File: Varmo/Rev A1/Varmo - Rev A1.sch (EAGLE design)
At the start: 73 parts, among them U1 ATMEGA328, U2 SN74LVC2G17DBVR, U3 SN74LVC2G17DBVR, U4 90814-0210, U5 90814-0210, U6 IRLML6344TRPBF, X1 NC5MAH, X2 SMKDSP_1,5/3, X3 SMKDSP_1,5/2, X4 SMKDSP_1,5/2, Y1 8MHz

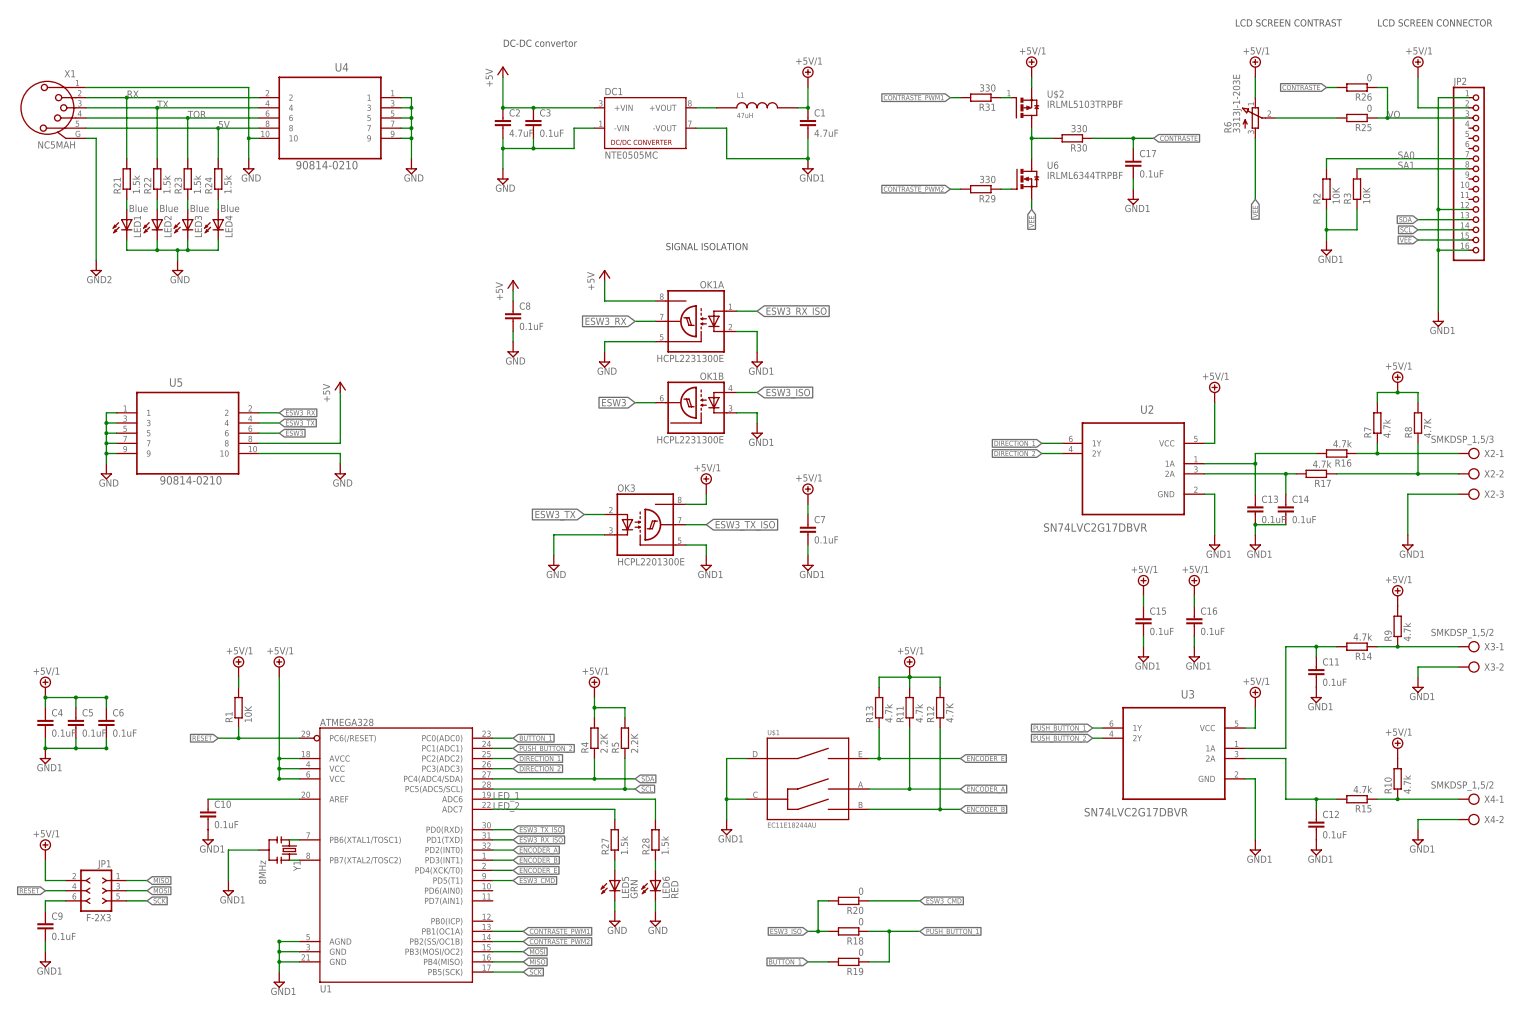
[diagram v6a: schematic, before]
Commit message: Update board of Varmo Rev 1, Update dc-dc-converter library
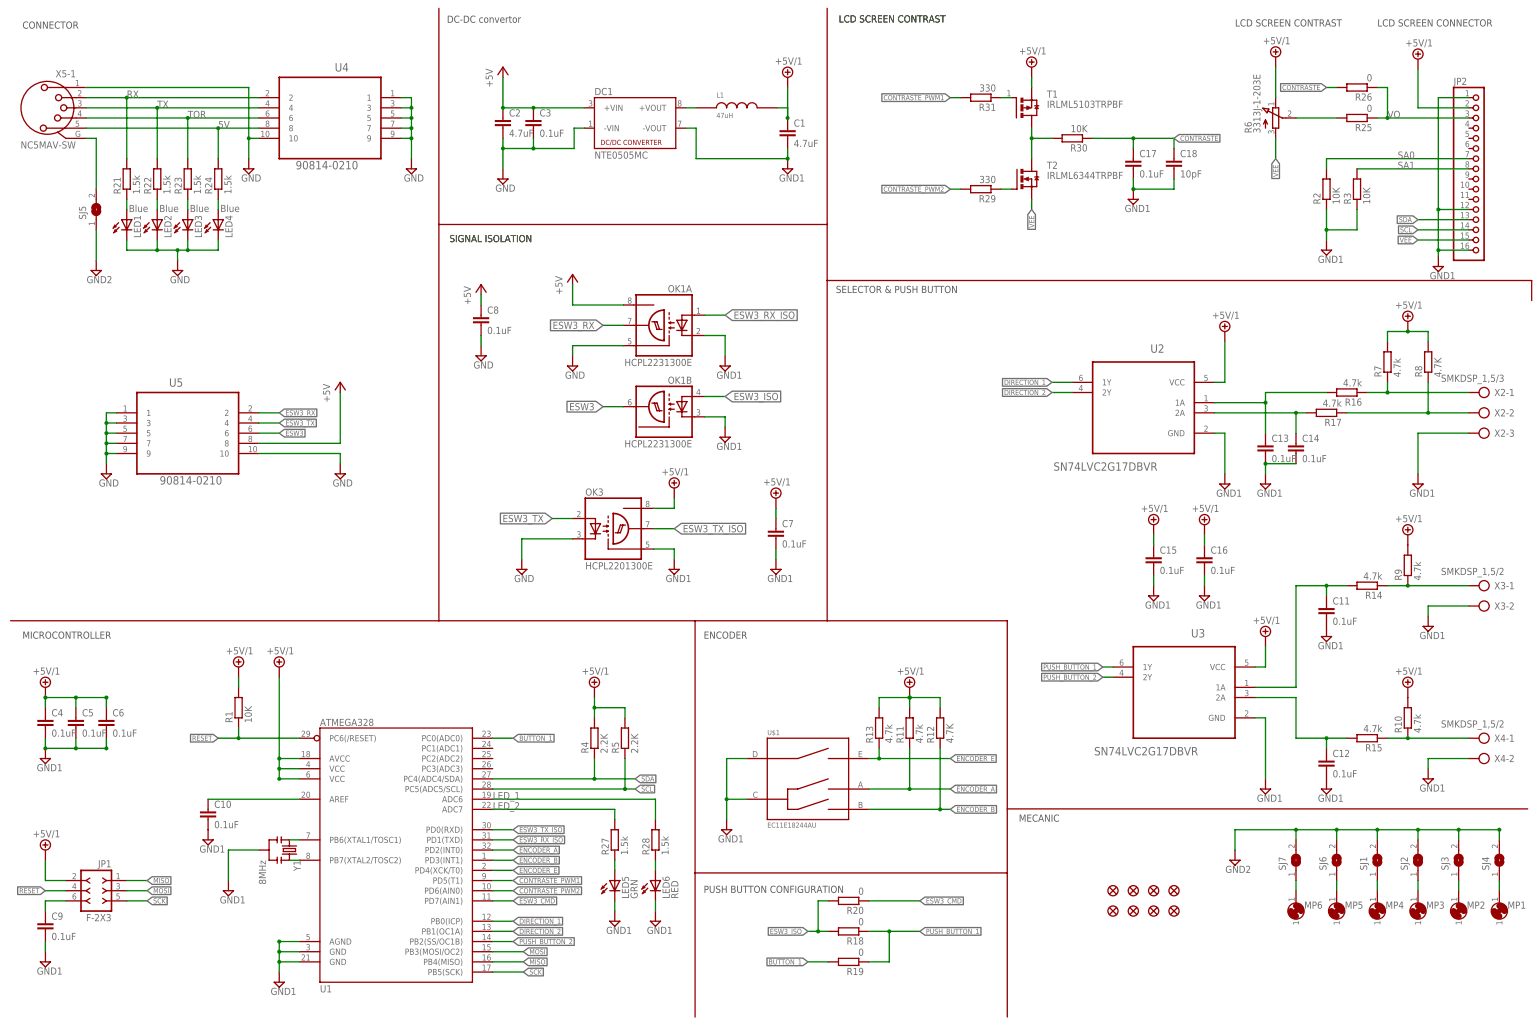
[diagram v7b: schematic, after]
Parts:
- removed X1: NC5MAH, con-neutrik_ag:NC5MAH
- added C18: 10pF, rcl:C-EUC0603
- added JP10, JP3, JP4, JP5, JP6, JP7, JP8, JP9: FIDUCIAL1X2, SparkFun:FIDUCIAL1X2
- added MP1, MP2, MP3, MP4, MP5, MP6: MOUNT-PAD3,0, holes:MOUNT-PAD3,0
- added SJ1, SJ2, SJ3, SJ4, SJ5, SJ6, SJ7: (no value), jumper:SJ
- added X5: NC5MAV-SW, con-neutrik_ag:NC5MAV-SW
- R30: value 330 -> 10K
- renumbered U$2 to T1, U6 to T2
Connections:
- new net 1: MP1.1, MP2.1, MP3.1, MP4.1, MP5.1, MP6.1, SJ1.1, SJ2.1, SJ3.1, SJ4.1, SJ6.1, SJ7.1
- new net N$23: SJ5.2, X5-1.G
- net 5V: now also X5-1.5; no longer X1.5
- net CONTRASTE: now also C18.1
- net CONTRASTE_PWM1: now also U1.PD5(T1); no longer U1.PB1(OC1A)
- net CONTRASTE_PWM2: now also U1.PD6(AIN0); no longer U1.PB2(SS/OC1B)
- net DIRECTION_1: now also U1.PB0(ICP); no longer U1.PC2(ADC2)
- net DIRECTION_2: now also U1.PB1(OC1A); no longer U1.PC3(ADC3)
- net ESW3_CMD: now also U1.PD7(AIN1); no longer U1.PD5(T1)
- net GND: now also X5-1.1; no longer LED5.C, LED6.C, X1.1
- net GND1: now also C18.2, LED5.C, LED6.C
- net GND2: now also SJ1.2, SJ2.2, SJ3.2, SJ4.2, SJ5.1, SJ6.2, SJ7.2; no longer X1.G
- net PUSH_BUTTON_2: now also U1.PB2(SS/OC1B); no longer U1.PC1(ADC1)
- net RX: now also X5-1.2; no longer X1.2
- net TOR: now also X5-1.4; no longer X1.4
- net TX: now also X5-1.3; no longer X1.3
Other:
- note added: "CONNECTOR"
- note added: "ENCODER"
- note added: "MECANIC"
- note added: "MICROCONTROLLER"
- note added: "PUSH BUTTON CONFIGURATION"
- note added: "SELECTOR & PUSH BUTTON"
- moved on the sheet: C1, C11, C12, C13, C14, C15, C16, C7, C8, DC1, L1, OK1A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

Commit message: Removed eagle.epf files, update Varmo Rev A1 schematic and board, add P2.5mm to holes.lbr, update midas.lbr
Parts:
- removed JP2: (no value), pinhead:PINHD-1X16
- removed LED6: RED, led:LED10MM
- removed MP1, MP2, MP3, MP4: MOUNT-PAD3,0, holes:MOUNT-PAD3,0
- removed R22, R23, R24: 1.5k, rcl:R-EU_R0603
- removed SJ1, SJ2, SJ3, SJ4: (no value), jumper:SJ
- added J1, J2: 22-05-7028-02, con-molex:22-05-7028-02
- added LCD1: MC21605G-VNMLWI, midas:MC21605G-VNMLWI
- added R32, R33, R34, R35: 1.5k, rcl:R-EU_R0603
- LED5: value GRN -> Green; device led:LED10MM -> led:LEDCHIP-LED0603
- MP5, MP6: value MOUNT-PAD3,0 -> MOUNT-PAD2.5; device holes:MOUNT-PAD3,0 -> holes:MOUNT-PAD2.5
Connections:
- removed net 5V: R24.2, U4.8, X5-1.5
- removed net GND2: SJ1.2, SJ2.2, SJ3.2, SJ4.2, SJ5.1, SJ6.2, SJ7.2
- removed net N$18: LED1.A, R21.1
- removed net N$19: LED2.A, R22.1
- removed net N$20: LED3.A, R23.1
- removed net N$21: LED4.A, R24.1
- removed net SA0: JP2.7, R2.2
- removed net SA1: JP2.8, R3.2
- new net N$29: LCD1.SA1, R2.2
- new net N$30: LCD1.SA0, R3.2
- new net N$31: LED1.A, R32.1
- new net N$32: LED2.A, R33.1
- new net N$33: LED3.A, R34.1
- new net N$34: LED4.A, R35.1
- new net N$35: LED5.A, R21.1
- net +5V: now also R35.2, U4.8, X5-1.5
- net +5V/1: now also LCD1.VDD, R21.2; no longer JP2.2
- net 1: no longer MP1.1, MP2.1, MP3.1, MP4.1, SJ1.1, SJ2.1, SJ3.1, SJ4.1
- net BUTTON_1: now also U1.ADC6; no longer U1.PC0(ADC0)
- net CONTRASTE_PWM1: now also U1.PD6(AIN0); no longer U1.PD5(T1)
- net CONTRASTE_PWM2: now also U1.PD5(T1); no longer U1.PD6(AIN0)
- net ESW3: now also R34.2
- net ESW3_RX: now also R33.2
- net ESW3_TX: now also R32.2
- net GND: now also SJ5.1
- net GND1: now also J1-2.S, J2-2.S, LCD1.CSB, LCD1.K, LCD1.VSS, SJ6.2, SJ7.2; no longer JP2.1, JP2.12, JP2.16, LED6.C
- net LED_1: now also U1.PC0(ADC0); no longer U1.ADC6
- net LED_2: now also U1.PC1(ADC1); no longer U1.ADC7
- net N$15: now also J2-1.S; no longer LED5.A
- net N$16: now also J1-1.S; no longer LED6.A
- net RX: no longer R21.2
- net SCL: now also LCD1.SCL; no longer JP2.14
- net SDA: now also LCD1.SDA; no longer JP2.13
- net TOR: no longer R23.2
- net TX: no longer R22.2
- net VEE: now also LCD1.VEE; no longer JP2.15
- net VO: now also LCD1.V0; no longer JP2.3
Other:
- moved on the sheet: C1, C17, C18, C2, C3, DC1, L1, LED1, LED2, LED3, LED4, LED5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
